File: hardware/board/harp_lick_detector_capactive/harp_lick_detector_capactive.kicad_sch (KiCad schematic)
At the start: 46 parts

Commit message: assign more components
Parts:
- R?: Link (none) -> https://www.digikey.com/en/products/detail/vishay-dale/RCS0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; Manufacturer (none) -> Vishay Dale; Manufacturer Number (none) -> RCS06036K19FKEA; Tolerance (none) -> 1%
- R?: Link (none) -> https://www.digikey.com/en/products/detail/yageo/RC0603FR-0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; Manufacturer (none) -> Yageo; Manufacturer Number (none) -> RC0603FR-079K76L; Tolerance (none) -> 1%
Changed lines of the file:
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@@
       (effects (font (size 1.27 1.27)) hide)
     )
-    (property "Datasheet" "~" (id 3) (at 140.97 64.77 0)
+    (property "Datasheet" "https://www.vishay.com/docs/20065/rcse3.pdf" (id 3) (at 140.97 64.77 0)
+      (effects (font (size 1.27 1.27)) hide)
+    )
+    (property "Link" "https://www.digikey.com/en/products/detail/vishay-dale/RCS06036K19FKEA/5868569" (id 4) (at 140.97 64.77 0)
+      (effects (font (size 1.27 1.27)) hide)
+    )
+    (property "Manufacturer" "Vishay Dale" (id 5) (at 140.97 64.77 0)
+      (effects (font (size 1.27 1.27)) hide)
+    )
+    (property "Manufacturer Number" "RCS06036K19FKEA" (id 6) (at 140.97 64.77 0)
+      (effects (font (size 1.27 1.27)) hide)
+    )
+    (property "Tolerance" "1%" (id 7) (at 140.97 64.77 0)
       (effects (font (size 1.27 1.27)) hide)
     )
@@
       (effects (font (size 1.27 1.27)) hide)
     )
-    (property "Datasheet" "~" (id 3) (at 151.13 64.77 0)
+    (property "Datasheet" "https://www.yageo.com/upload/media/product/productsearch/datasheet/rchip/PYu-RC_Group_51_RoHS_L_12.pdf" (id 3) (at 151.13 64.77 0)
+      (effects (font (size 1.27 1.27)) hide)
+    )
+    (property "Link" "https://www.digikey.com/en/products/detail/yageo/RC0603FR-079K76L/727422" (id 4) (at 151.13 64.77 0)
+      (effects (font (size 1.27 1.27)) hide)
+    )
+    (property "Manufacturer" "Yageo" (id 5) (at 151.13 64.77 0)
+      (effects (font (size 1.27 1.27)) hide)
+    )
+    (property "Manufacturer Number" "RC0603FR-079K76L" (id 6) (at 151.13 64.77 0)
+      (effects (font (size 1.27 1.27)) hide)
+    )
+    (property "Tolerance" "1%" (id 7) (at 151.13 64.77 0)
       (effects (font (size 1.27 1.27)) hide)
     )
@@
     )
     (path "/68ba3686-54f3-42b1-847b-d7576a207bac/de90e053-997b-4c00-9ded-500b48b5298c"
-      (reference "J2") (unit 1) (value "USB_C_Receptacle_USB2.0") (footprint "Connector_USB:USB_C_Receptacle_Amphenol_12401610E4-2A_CircularHoles")
+      (reference "J2") (unit 1) (value "USB_C_Receptacle_USB2.0") (footprint "")
     )
     (path "/e4a7aee0-dcfb-4235-9742-83dd7c58f1df"
@@
     )
     (path "/32f9365a-e60e-47d3-bd67-aeb1f7f06f62"
-      (reference "R?") (unit 1) (value "6K19") (footprint "")
+      (reference "R?") (unit 1) (value "6K19") (footprint "Resistor_SMD:R_0603_1608Metric_Pad0.98x0.95mm_HandSolder")
     )
     (path "/44108556-aea5-45b3-9fd6-96c6349a5776"
-      (reference "R?") (unit 1) (value "9K76") (footprint "")
+      (reference "R?") (unit 1) (value "9K76") (footprint "Resistor_SMD:R_0603_1608Metric_Pad0.98x0.95mm_HandSolder")
     )
     (path "/631fccd5-5f59-4c03-8d5f-b57213e41c21"
@@
     )
     (path "/faa455ea-93b0-4a12-9af2-c32e7eee6d37/ba8fbee5-4b7d-4129-8b40-a6635bf7962c"
-      (reference "R?") (unit 1) (value "5.1") (footprint "")
+      (reference "R?") (unit 1) (value "5.1") (footprint "Resistor_SMD:R_0603_1608Metric_Pad0.98x0.95mm_HandSolder")
     )
     (path "/68ba3686-54f3-42b1-847b-d7576a207bac/e076d21d-ef49-470c-8b00-c8bbf7e83a74"
@@
     )
     (path "/faa455ea-93b0-4a12-9af2-c32e7eee6d37/8754c8ad-8208-4779-a399-e236a119fdb3"
-      (reference "U3") (unit 1) (value "ADA4807-2ARM") (footprint "")
+      (reference "U3") (unit 1) (value "ADA4807-2ARM") (footprint "Package_SO:MSOP-8_3x3mm_P0.65mm")
     )
     (path "/faa455ea-93b0-4a12-9af2-c32e7eee6d37/5409cc31-4322-4031-ade5-4014b3199ad7"
-      (reference "U3") (unit 2) (value "ADA4807-2ARM") (footprint "")
+      (reference "U3") (unit 2) (value "ADA4807-2ARM") (footprint "Package_SO:MSOP-8_3x3mm_P0.65mm")
     )
     (path "/faa455ea-93b0-4a12-9af2-c32e7eee6d37/710a902c-a359-4d20-89a3-7c2b1217c470"
-      (reference "U3") (unit 3) (value "ADA4807-2ARM") (footprint "")
+      (reference "U3") (unit 3) (value "ADA4807-2ARM") (footprint "Package_SO:MSOP-8_3x3mm_P0.65mm")
     )
     (path "/faa455ea-93b0-4a12-9af2-c32e7eee6d37/246dc4eb-2f40-436e-9de0-58f0d1dabd22"
-      (reference "U4") (unit 1) (value "AD9833xRM") (footprint "")
+      (reference "U4") (unit 1) (value "AD9833xRM") (footprint "Package_SO:MSOP-10_3x3mm_P0.5mm")
     )
     (path "/899e7de8-aee4-403a-b9d1-10a87b85205e"
@@
     )
     (path "/68ba3686-54f3-42b1-847b-d7576a207bac/a9f1a520-788a-4900-a012-44a537e52ba3"
-      (reference "U7") (unit 1) (value "W25Q128JVS") (footprint "")
+      (reference "U7") (unit 1) (value "W25Q128JVS") (footprint "Package_SO:SOIC-8_5.23x5.23mm_P1.27mm")
     )
     (path "/68ba3686-54f3-42b1-847b-d7576a207bac/43250aa1-3e53-4e19-90f2-2c7939b02062"

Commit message: complete bom draft
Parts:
- added C? (x2): (no value), symbol Device:C
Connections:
- net +5V: now also C?.2
- net -5V: now also C?.1
- net GND: now also C?.1, C?.2
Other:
- note added: "ADA4807-4 Bypass Caps"
- note added: "DC Offset: 1.65V"
- note removed: "1.65[v] DC offset"
- moved on the sheet: C?, D1, J1, J3, J4, JP1, JP2, R?, RN1A, RN1B, RN1C, RN1D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

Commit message: add precision oscillator
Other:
- note added: "Sensing Front End"
- note added: "TODO: Consider TTL Lick output"
- note removed: "Sensing"

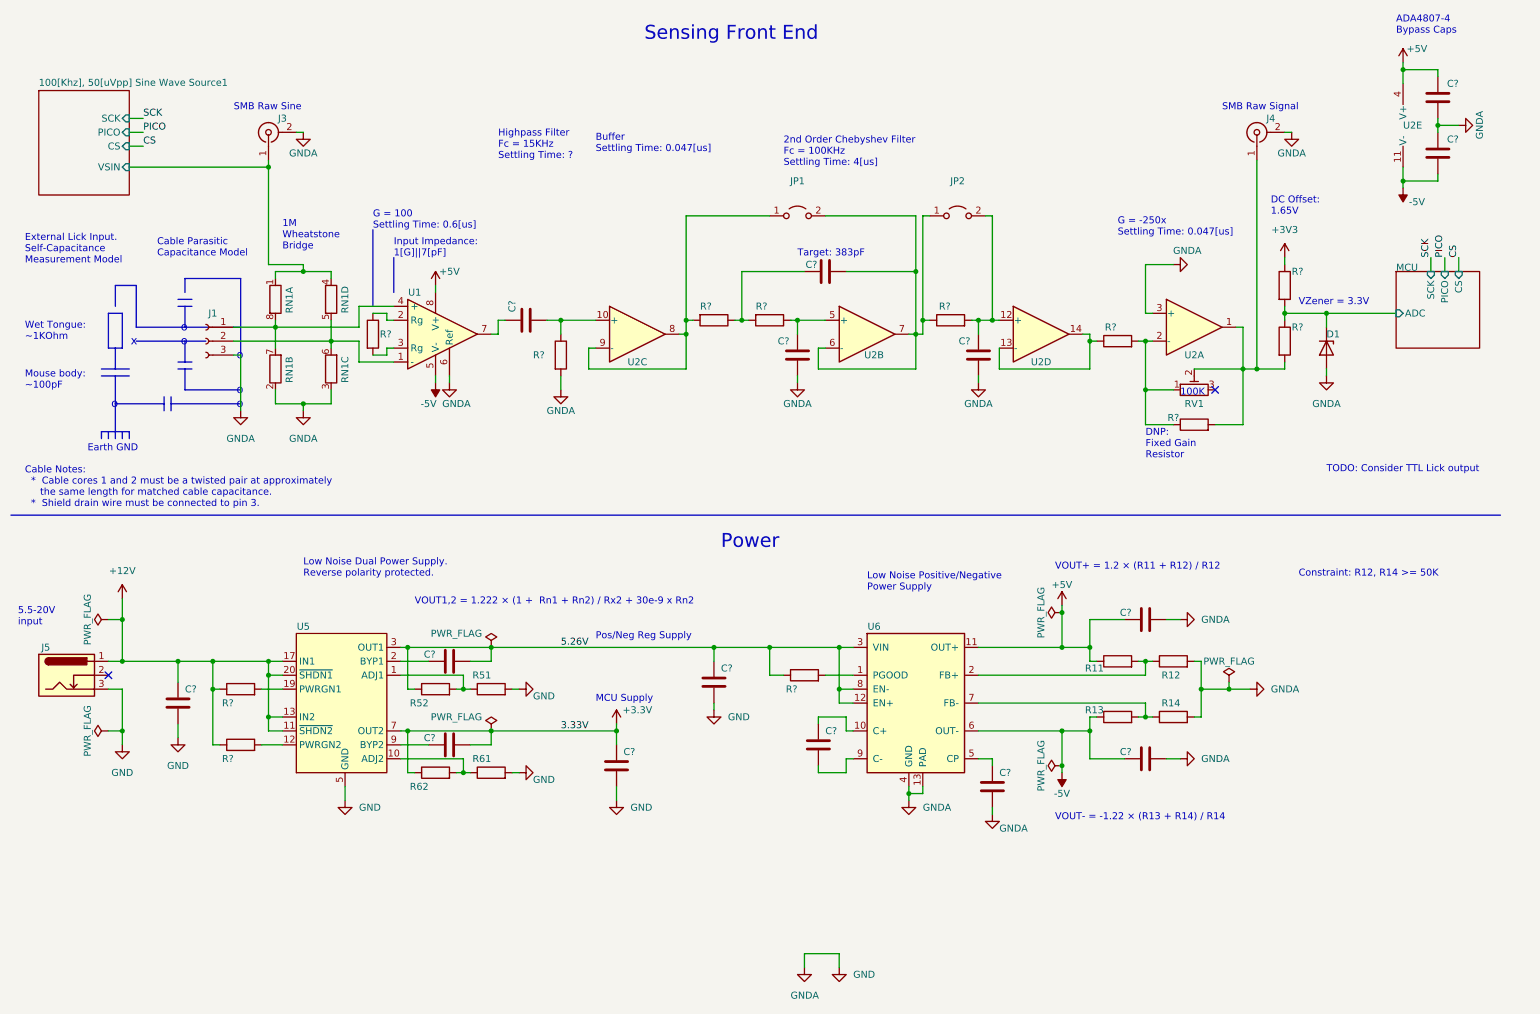
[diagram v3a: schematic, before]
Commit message: add usb isolator
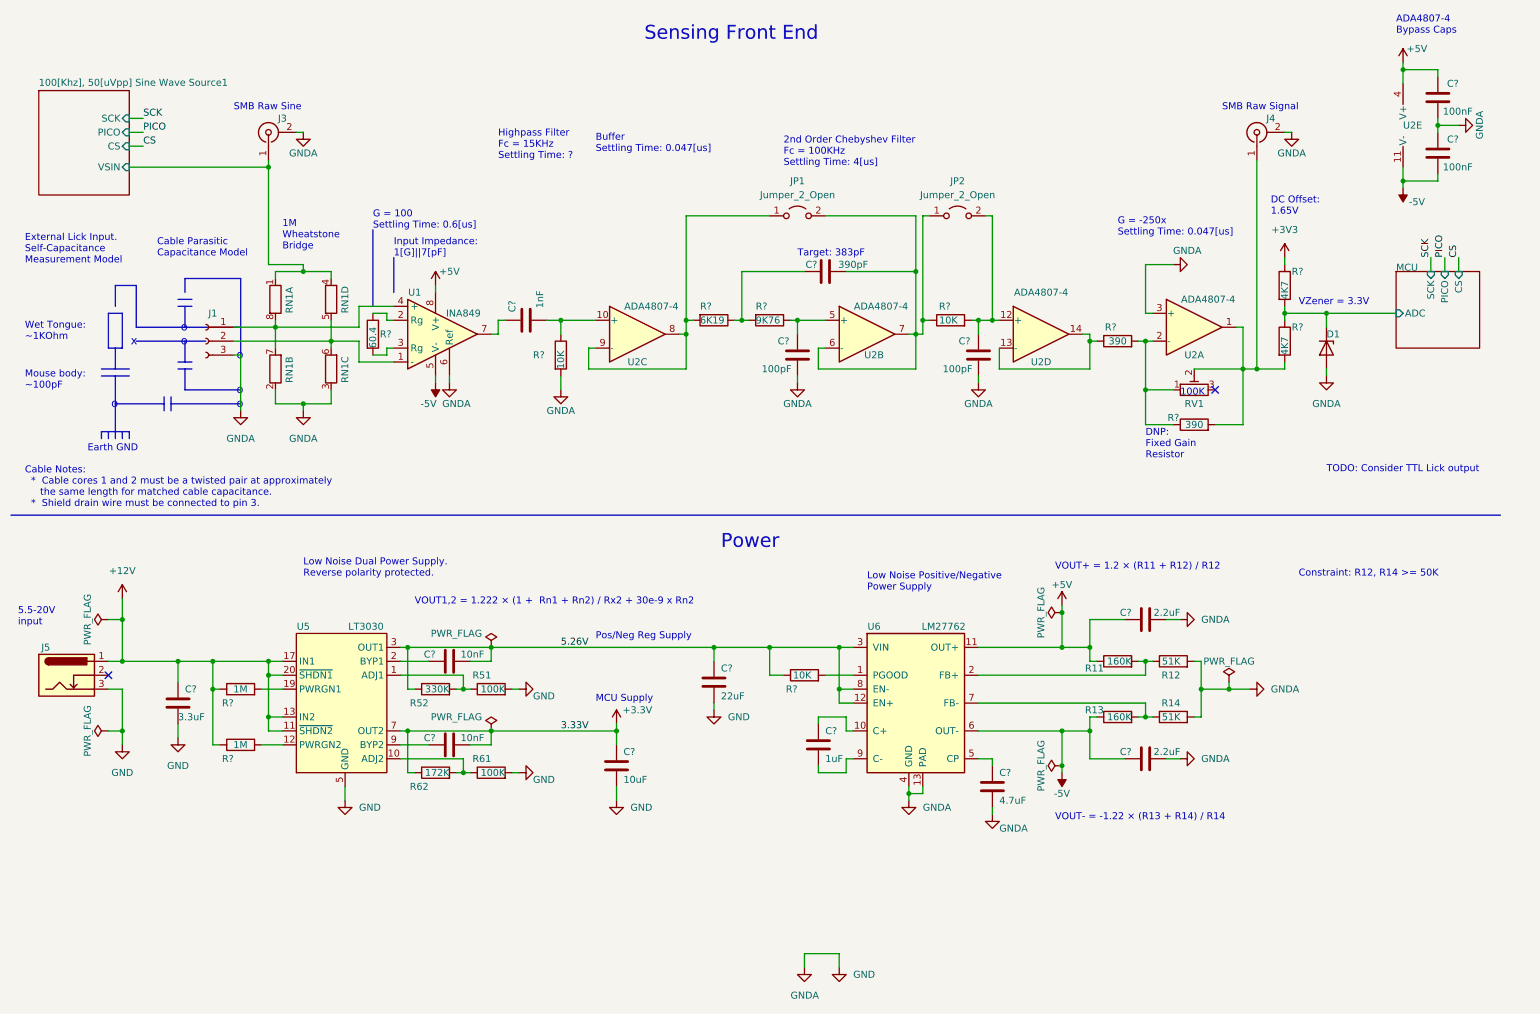
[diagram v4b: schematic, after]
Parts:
- C?: value (none) -> 1uF; footprint (none) -> Capacitor_SMD:C_0603_1608Metric_Pad1.08x0.95mm_HandSolder
- C?: value (none) -> 3.3uF; footprint (none) -> Capacitor_SMD:C_0805_2012Metric_Pad1.18x1.45mm_HandSolder
- C? (x2): value (none) -> 100nF; footprint (none) -> Capacitor_SMD:C_0603_1608Metric_Pad1.08x0.95mm_HandSolder
- C?: value (none) -> 1nF; footprint (none) -> Capacitor_SMD:C_0603_1608Metric_Pad1.08x0.95mm_HandSolder
- C?: value (none) -> 22uF; footprint (none) -> Capacitor_SMD:C_0805_2012Metric_Pad1.18x1.45mm_HandSolder
- C? (x2): value (none) -> 2.2uF; footprint (none) -> Capacitor_SMD:C_0603_1608Metric_Pad1.08x0.95mm_HandSolder
- C? (x2): value (none) -> 100pF; footprint (none) -> Capacitor_SMD:C_0603_1608Metric_Pad1.08x0.95mm_HandSolder
- C?: value (none) -> 10uF; footprint (none) -> Capacitor_SMD:C_0805_2012Metric
- C?: value (none) -> 4.7uF; footprint (none) -> Capacitor_SMD:C_0805_2012Metric_Pad1.18x1.45mm_HandSolder
- C? (x2): value (none) -> 10nF; footprint (none) -> Capacitor_SMD:C_0603_1608Metric_Pad1.08x0.95mm_HandSolder
- C?: value (none) -> 390pF; footprint (none) -> Resistor_SMD:R_0402_1005Metric_Pad0.72x0.64mm_HandSolder
- D1: value (none) -> BZX384-A3V3-QX; footprint (none) -> Diode_SMD:D_SOD-323_HandSoldering
- J1: value (none) -> 3-Pin Connector Socket; footprint (none) -> Connector_Phoenix_MC:PhoenixContact_MC_1,5_3-G-3.5_1x03_P3.50mm_Horizontal
- J3, J4: value (none) -> Conn_Coaxial; footprint (none) -> Connector_Coaxial:SMA_Amphenol_901-143_Horizontal
- J5: value (none) -> Barrel_Jack_Switch_Pin3Ring
- JP1, JP2: value (none) -> Jumper_2_Open; footprint (none) -> Jumper:SolderJumper-2_P1.3mm_Open_RoundedPad1.0x1.5mm
- R11, R13: value (none) -> 160K; footprint (none) -> Resistor_SMD:R_0603_1608Metric_Pad0.98x0.95mm_HandSolder
- R12, R14: value (none) -> 51K; footprint (none) -> Resistor_SMD:R_0603_1608Metric_Pad0.98x0.95mm_HandSolder
- R51, R61: value (none) -> 100K; footprint (none) -> Capacitor_SMD:C_0603_1608Metric_Pad1.08x0.95mm_HandSolder
- R52: value (none) -> 330K; footprint (none) -> Resistor_SMD:R_0603_1608Metric_Pad0.98x0.95mm_HandSolder
- R62: value (none) -> 172K; footprint (none) -> Resistor_SMD:R_0603_1608Metric_Pad0.98x0.95mm_HandSolder
- R? (x3): value (none) -> 10K; footprint (none) -> Resistor_SMD:R_0402_1005Metric_Pad0.72x0.64mm_HandSolder
- R?: value (none) -> 6K19; footprint (none) -> Resistor_SMD:R_0603_1608Metric_Pad0.98x0.95mm_HandSolder
- R?: value (none) -> 9K76; footprint (none) -> Resistor_SMD:R_0603_1608Metric_Pad0.98x0.95mm_HandSolder
- R? (x2): value (none) -> 390; footprint (none) -> Resistor_SMD:R_0603_1608Metric_Pad0.98x0.95mm_HandSolder
- R? (x2): value (none) -> 1M; footprint (none) -> Resistor_SMD:R_0603_1608Metric_Pad0.98x0.95mm_HandSolder
- R? (x2): value (none) -> 4K7; footprint (none) -> Resistor_SMD:R_0603_1608Metric_Pad0.98x0.95mm_HandSolder
- R?: value (none) -> 60.4; footprint (none) -> Resistor_SMD:R_0603_1608Metric_Pad0.98x0.95mm_HandSolder
- RN1: value (none) -> R_Pack04_Split; footprint (none) -> Package_SO:MSOP-8_3x3mm_P0.65mm
- RV1: value (none) -> R_Potentiometer_Trim; footprint (none) -> Potentiometer_SMD:Potentiometer_Bourns_3314G_Vertical
- U1: value (none) -> INA849; footprint (none) -> Package_SO:SOIC-8-1EP_3.9x4.9mm_P1.27mm_EP2.29x3mm
- U2: value (none) -> ADA4807-4; footprint (none) -> Package_SO:TSSOP-14_4.4x5mm_P0.65mm
- U5: value (none) -> LT3030; footprint (none) -> Package_SO:TSSOP-20_4.4x6.5mm_P0.65mm
- U6: value (none) -> LM27762; footprint (none) -> Package_SON:WSON-12-1EP_3x2mm_P0.5mm_EP1x2.65_ThermalVias
